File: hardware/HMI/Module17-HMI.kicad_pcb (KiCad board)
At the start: 4 copper layers, 91.5 x 80 mm, 59 parts, among them J1 Hirose FH12-26S-0.5SH(55), J3 Hirose FH12A-24S-0.5SH(55), Q1 MMBT3904, Q2 BSS84, SW9 CL-SB-22A-1x, U1 TPS61040DBV, U2 AP7375-33SA, U3 IQS211B00000000TS, U4 CAP1206-x-SL

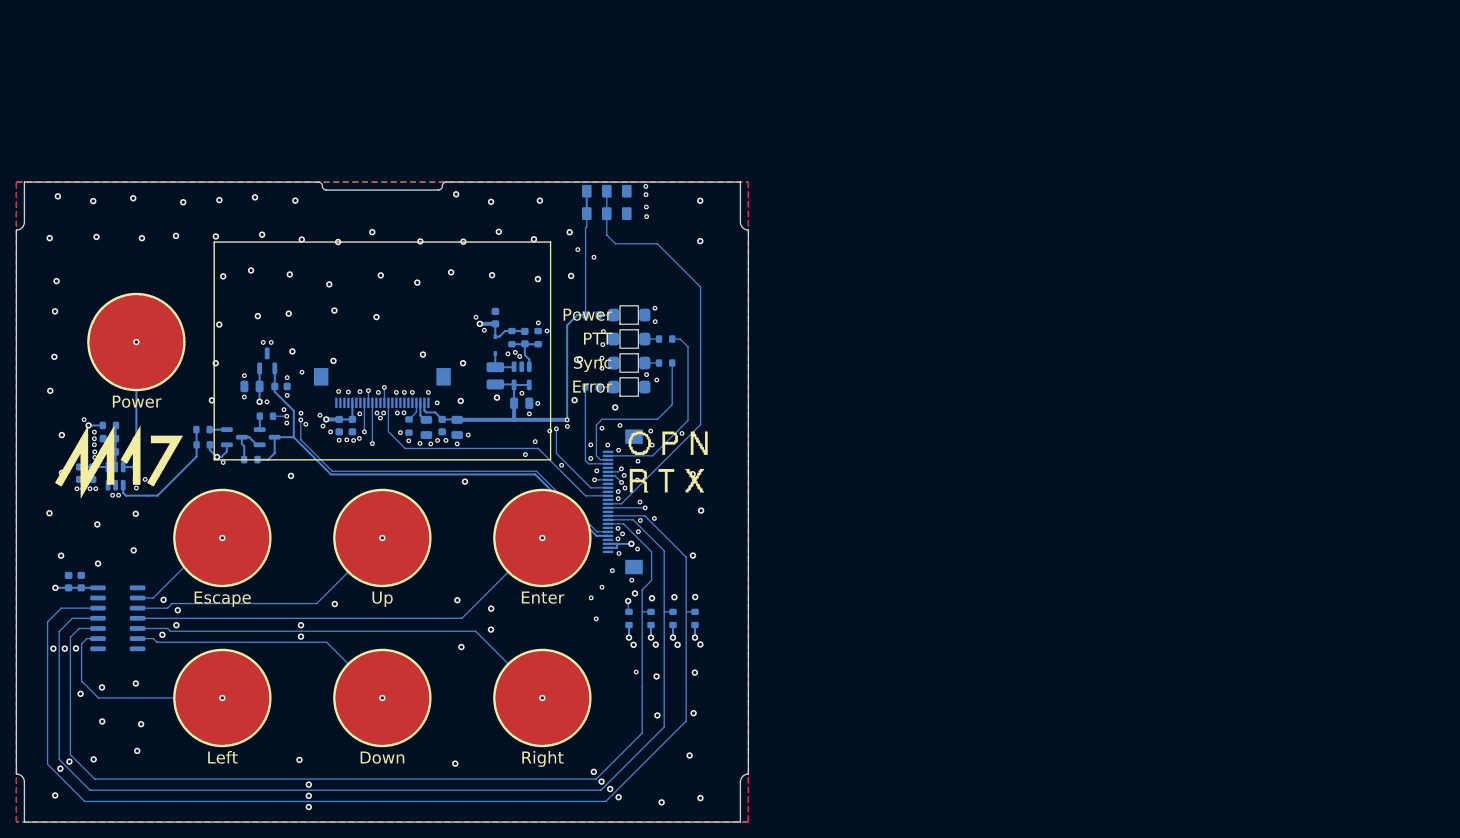
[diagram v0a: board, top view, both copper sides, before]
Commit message: Updated HMI boards
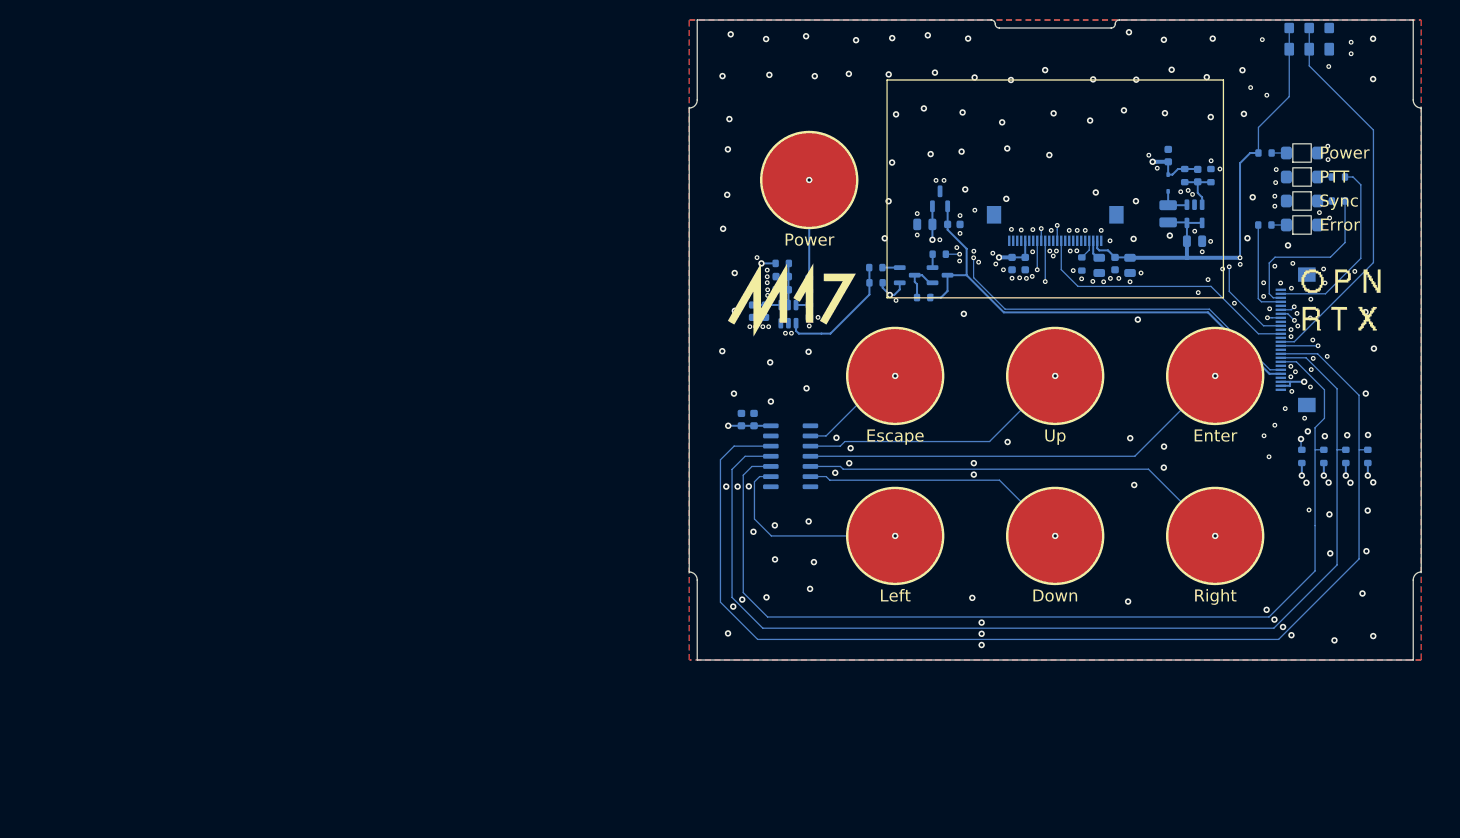
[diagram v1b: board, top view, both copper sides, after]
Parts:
- SW9: footprint M17_misc_passive:Nidec_Copal-SB-22A -> M17_misc_passive:Nidec_Copal-SB-22A_edge
- moved SW9 90.2 mm to (243.2, 46.7)
- moved C1 86.5 mm to (228.9, 72.1)
- moved C12 86.5 mm to (180.7, 80.9)
- moved C13 86.5 mm to (207.7, 74.9)
- moved C14 86.5 mm to (217.0, 75.2)
- moved C16 86.5 mm to (220.8, 75.2)
- moved C17 86.5 mm to (218.9, 74.9)
- moved C2 86.5 mm to (229.3, 63.9)
- moved C3 86.5 mm to (225.6, 61.4)
- moved C5 86.5 mm to (177.3, 78.2)
- moved C6 86.5 mm to (177.3, 76.6)
- moved D2 86.5 mm to (242.3, 61.1)
- moved D3 86.5 mm to (242.3, 64.1)
- moved D4 86.5 mm to (242.3, 67.1)
- moved D5 86.5 mm to (242.3, 70.1)
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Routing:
- net ESC/BOOT0: track 52.3 -> 48.3 mm
- net VCC: track 189.7 -> 191.8 mm
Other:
- outline, holes or cut-outs redrawn
- board text added: "0.1500 mm / 0.1500 mm"
- board text added: "0.3000 mm"
- board text added: "1.6000 mm"
- board text added: "4"
- board text added: "91.5000 mm x 80.0000 mm"
- board text added: "All vias should be filled and capped. There are no PTH in this design."
- board text added: "BOARD CHARACTERISTICS"
- board text added: "Board Thickness:"
- board text added: "Board overall dimensions:"
- board text added: "Castellated pads:"
- board text added: "Copper Layer Count:"
- board text added: "Edge card connectors:"
- board text added: "Impedance Control:"
- board text added: "JLCJLCJLCJLC"
- board text added: "Min hole diameter:"
- board text added: "Min track/spacing:"
- board text added: "No"
- board text added: "Plated Board Edge:"

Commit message: Updated HMI
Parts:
- SW9: value CL-SB-22A-1x -> CL-SB-22A-11T
- moved C16 17.8 mm to (203.0, 75.5)
- moved C17 14.1 mm to (204.9, 75.3)
- moved C15 10.7 mm to (216.8, 75.2)
- moved C14 10.2 mm to (206.7, 75.5)
- moved C13 7.50 mm to (215.2, 75.2)
- moved R8 6.23 mm to (208.6, 75.3)
- moved SW8 1.38 mm to (179.3, 64.5)
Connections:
- C14 pad 1: Net-(J3-Pin_22) -> Net-(J3-Pin_3)
- J3 pad 10: OLED_DC -> unconnected-(J3-Pin_10-Pad10)
- J3 pad 11: GND -> OLED_SPI_MOSI
- J3 pad 12: GND -> OLED_SPI_SCK
- J3 pad 13: OLED_SPI_SCK -> GND
- J3 pad 14: OLED_SPI_MOSI -> GND
- J3 pad 15: unconnected-(J3-Pin_15-Pad15) -> OLED_DC
- J3 pad 16: GND -> OLED_RST
- J3 pad 17: GND -> OLED_CS
- J3 pad 2: GND -> VCC
- J3 pad 20: GND -> VDD
- J3 pad 21: Net-(J3-Pin_21) -> GND
- J3 pad 22: Net-(J3-Pin_22) -> GND
- J3 pad 23: VCC -> GND
- J3 pad 3: GND -> Net-(J3-Pin_3)
- J3 pad 4: GND -> Net-(J3-Pin_4)
- J3 pad 5: VDD -> GND
- J3 pad 8: OLED_CS -> GND
- J3 pad 9: OLED_RST -> GND
- R8 pad 1: Net-(J3-Pin_21) -> Net-(J3-Pin_4)
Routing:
- net VCC: track 191.8 -> 215.8 mm, vias 7 -> 9
- net VDD: track 38.7 -> 27.6 mm
- net OLED_RST: track 39.2 -> 32.8 mm, vias 2 -> 0
- net GND: track 0.00 -> 6.03 mm, vias 234 -> 258
- net OLED_DC: track 40.5 -> 34.6 mm, vias 2 -> 0
- net OLED_SPI_MOSI: track 34.4 -> 38.9 mm
- net Net-(J3-Pin_4): track 0.00 -> 2.91 mm
- net Net-(J3-Pin_22): track 2.57 -> 0.00 mm
- net Net-(J3-Pin_21): track 2.46 -> 0.00 mm
- net Net-(J3-Pin_3): track 0.00 -> 2.45 mm
- net OLED_CS: track 37.7 -> 39.1 mm
- net Net-(R7-Pad2): track 12.2 -> 12.8 mm
- net HMI_PWR_ON: track 49.3 -> 49.9 mm
- net OLED_SPI_SCK: track 36.9 -> 36.6 mm, vias 2 -> 0
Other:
- board text added: "FW Update"
- board text added: "Run Mode"

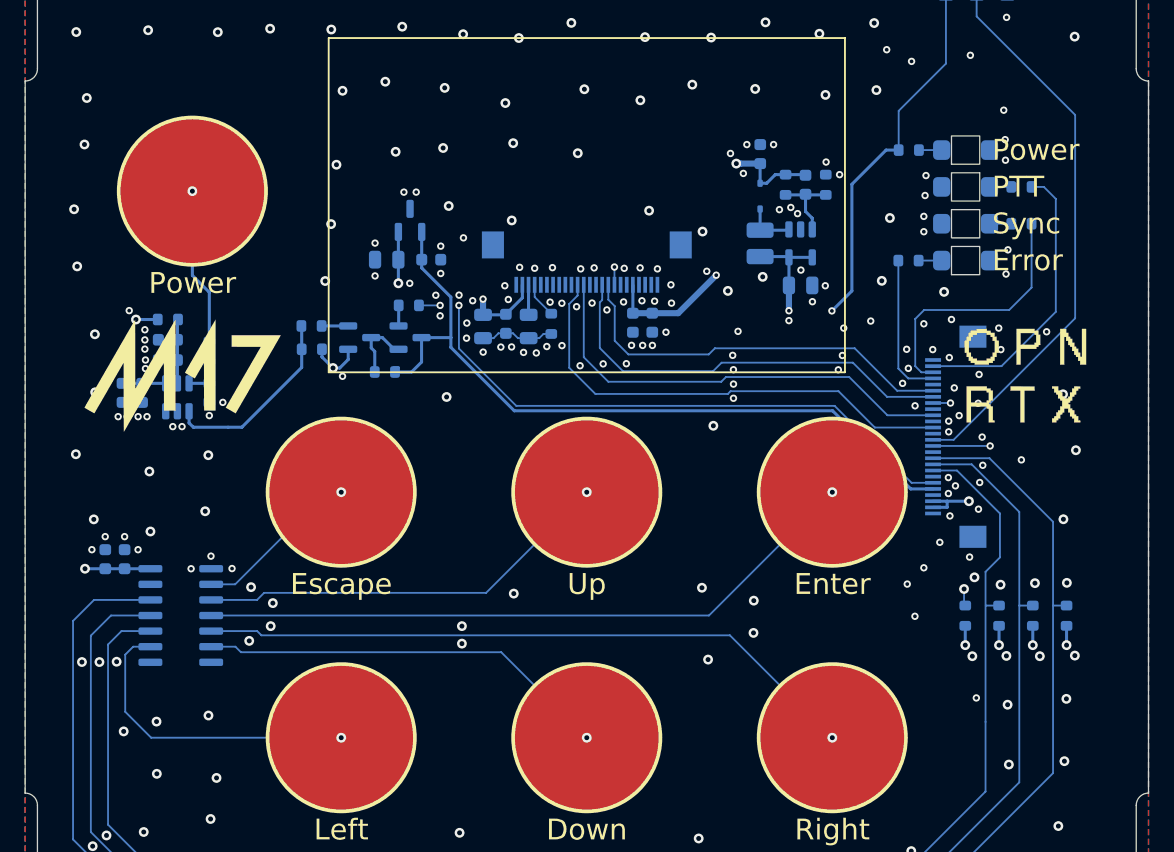
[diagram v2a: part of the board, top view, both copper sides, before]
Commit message: Updated HMI top panel
Removed soldermask on the edges, added some vias, updated LED footprints plus misc. changes
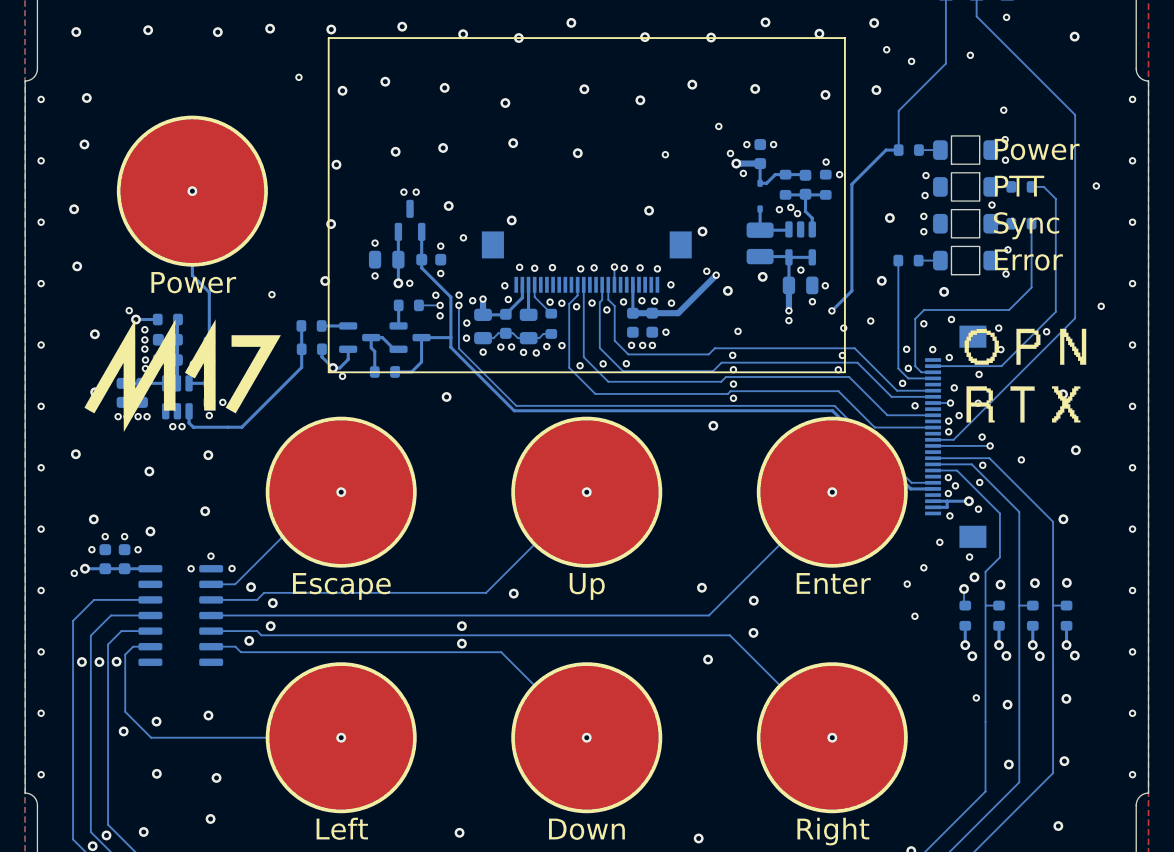
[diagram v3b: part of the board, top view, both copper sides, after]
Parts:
- R4: value 40R -> 40.2
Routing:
- net GND: vias 258 -> 292
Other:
- board text added: "If tooling holes or fiducials are to be added, they have to be added on the rails placed for assembly."

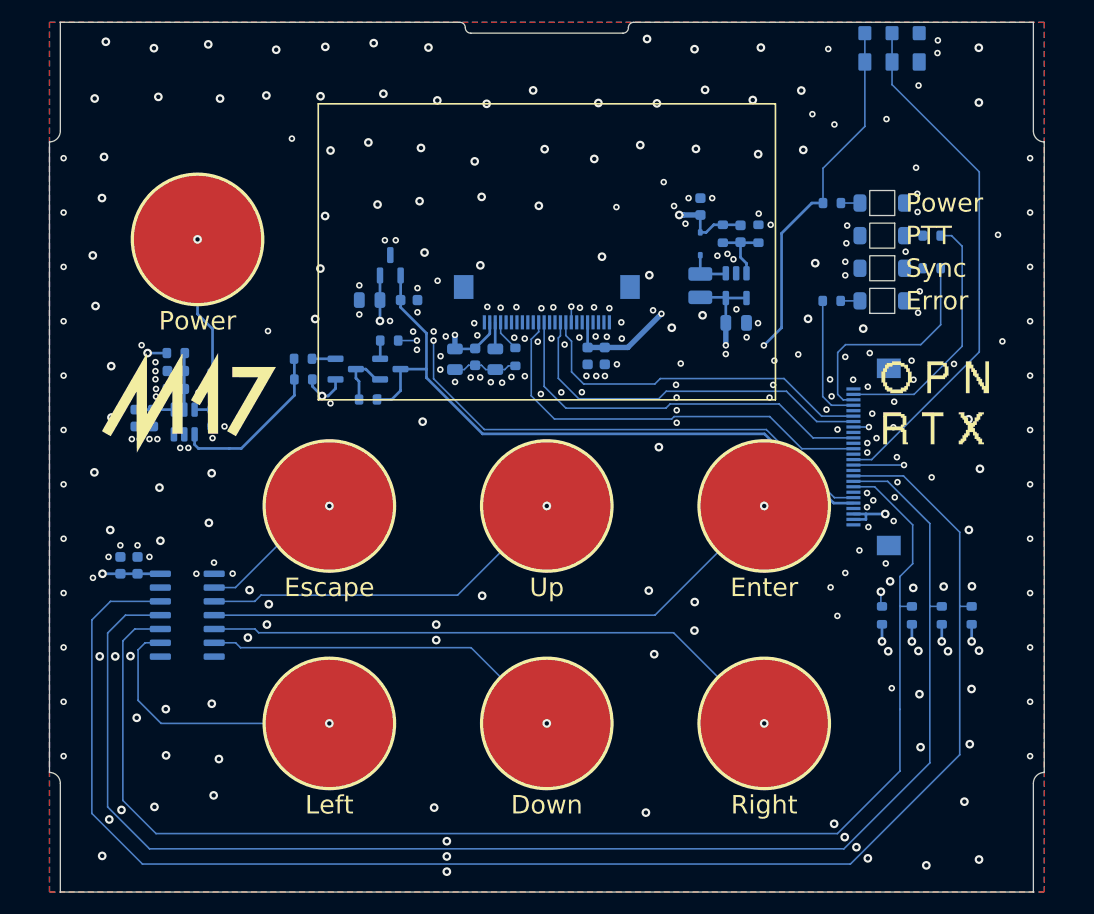
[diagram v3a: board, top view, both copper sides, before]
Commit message: Updated HMI board
Fixed OLED screen power supply (VCC/VDD swapped).
Fixed Mainboard connector pinout.
Widened board.
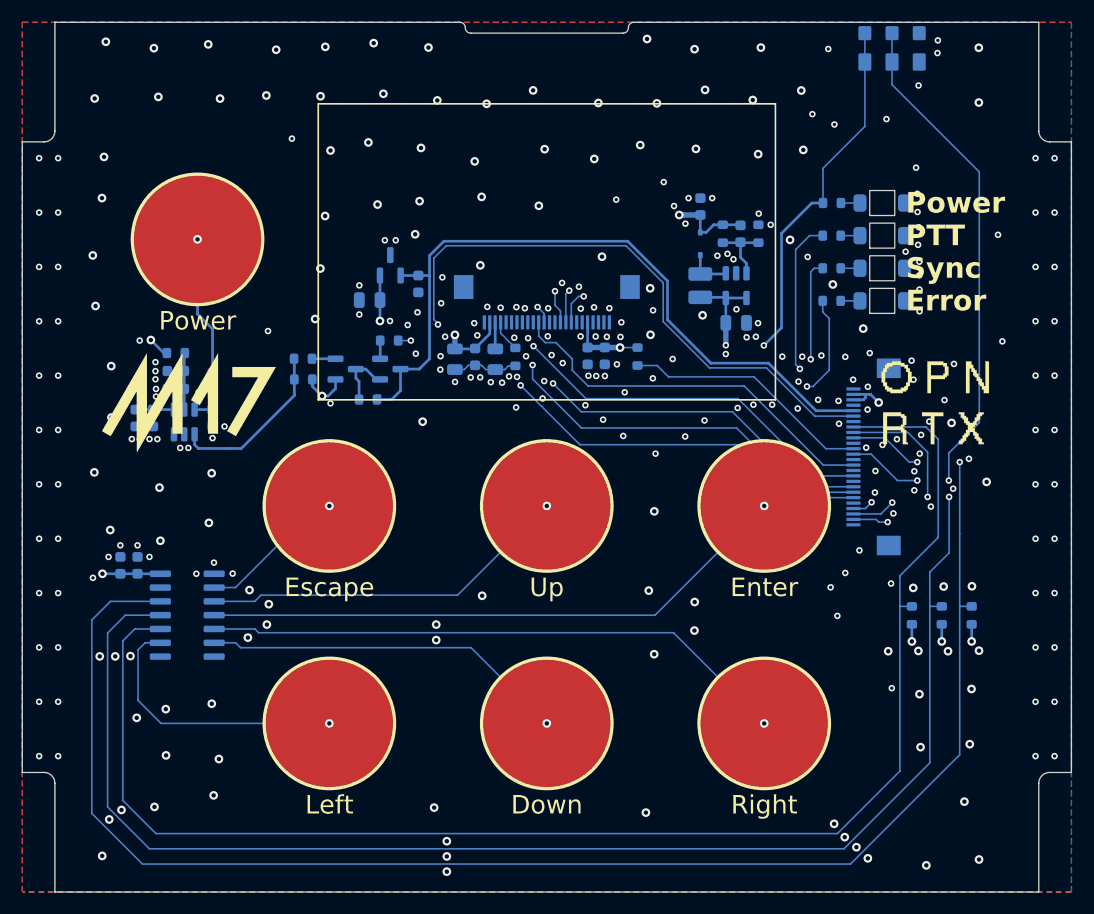
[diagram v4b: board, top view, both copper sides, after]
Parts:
- R8: value 910k -> 953k
- moved R17 32.7 mm to (219.8, 75.2), turned to -90 degrees
- moved R10 9.20 mm to (237.7, 64.1), turned to 0 degrees
- moved R11 9.20 mm to (237.7, 67.1), turned to 0 degrees
- moved C4 1.71 mm to (199.6, 68.6), turned to -90 degrees
- turned D3 to 0 degrees
- turned D4 to 0 degrees
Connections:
- C13 pad 1: VDD -> VCC
- C15 pad 1: VDD -> VCC
- C16 pad 1: VCC -> VDD
- C17 pad 1: VCC -> VDD
- J1 pad 10: OLED_SPI_SCK -> SMCLK
- J1 pad 11: GND -> unconnected-(J1-Pin_11-Pad11)
- J1 pad 12: OLED_SPI_MOSI -> Net-(J1-Pin_12)
- J1 pad 13: GND -> ESC/BOOT0
- J1 pad 14: ESC/BOOT0 -> GND
- J1 pad 15: Net-(J1-Pin_15) -> OLED_SPI_MOSI
- J1 pad 16: unconnected-(J1-Pin_16-Pad16) -> GND
- J1 pad 17: SMCLK -> OLED_SPI_SCK
- J1 pad 18: SMDATA -> GND
- J1 pad 19: SMBA -> OLED_CS
- J1 pad 2: LED_PTT -> VCC
- J1 pad 20: GND -> OLED_DC
- J1 pad 21: HMI_PWR_ON -> OLED_RST
- J1 pad 22: HMI_VIN -> GND
- J1 pad 23: GND -> LED_ERROR
- J1 pad 24: VCC -> LED_SYNC
- J1 pad 25: VCC -> LED_PTT
- J1 pad 3: LED_SYNC -> VCC
- J1 pad 4: LED_ERROR -> GND
- J1 pad 5: GND -> HMI_VIN
- J1 pad 6: OLED_RST -> HMI_PWR_ON
- J1 pad 7: OLED_DC -> GND
- J1 pad 8: OLED_CS -> SMBA
- J1 pad 9: GND -> SMDATA
- J3 pad 2: VCC -> VDD
- J3 pad 20: VDD -> VCC
- R17 pad 2: Net-(J1-Pin_15) -> Net-(J1-Pin_12)
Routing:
- net Net-(J1-Pin_12): track 0.00 -> 23.0 mm
- net VCC: track 215.8 -> 196.7 mm, vias 9 -> 8
- net Net-(J1-Pin_15): track 18.8 -> 0.00 mm, vias 2 -> 0
- net OLED_RST: track 32.8 -> 49.0 mm, vias 0 -> 2
- net LED_ERROR: track 12.0 -> 24.3 mm, vias 0 -> 2
- net LED_PTT: track 23.4 -> 35.1 mm, vias 0 -> 2
- net VDD: track 27.6 -> 39.2 mm
- net OLED_DC: track 34.6 -> 45.8 mm, vias 0 -> 2
- net SMBA: track 124.8 -> 135.0 mm
- net LED_SYNC: track 21.2 -> 29.6 mm, vias 0 -> 2
- net HMI_PWR_ON: track 49.9 -> 58.2 mm
- net SMDATA: track 133.7 -> 141.9 mm, vias 0 -> 2
- net ESC/BOOT0: track 48.3 -> 55.4 mm, vias 0 -> 2
- net HMI_VIN: track 61.3 -> 68.1 mm
- net SMCLK: track 144.1 -> 149.3 mm, vias 0 -> 2
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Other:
- board size 91.5 x 80 mm -> 96.5 x 80 mm
